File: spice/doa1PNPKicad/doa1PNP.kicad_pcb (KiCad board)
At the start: 2 copper layers, 27 parts, among them Q1 BC547, Q2 BC557, Q3 BC557, Q4 BC557, Q5 BC547, Q6 BC557, Q7 BC547

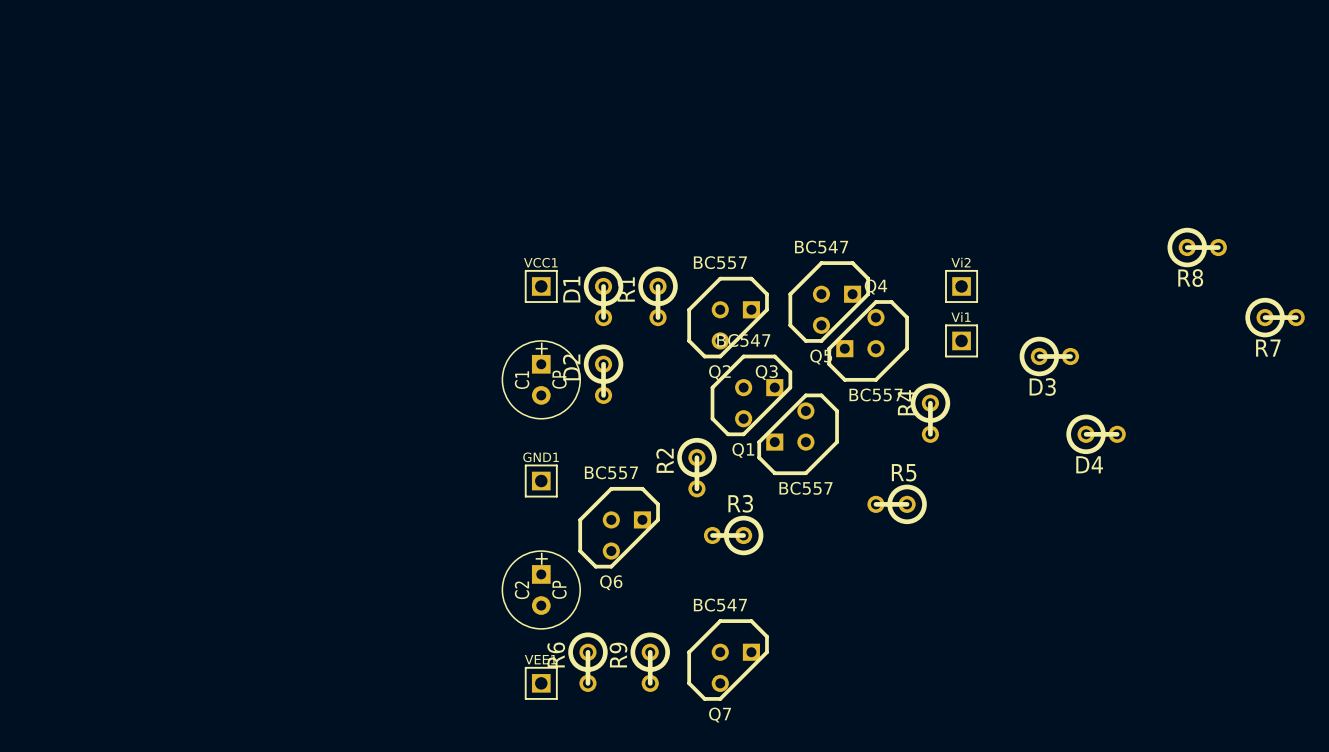
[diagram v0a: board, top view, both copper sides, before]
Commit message: multiple current source doa1PNP
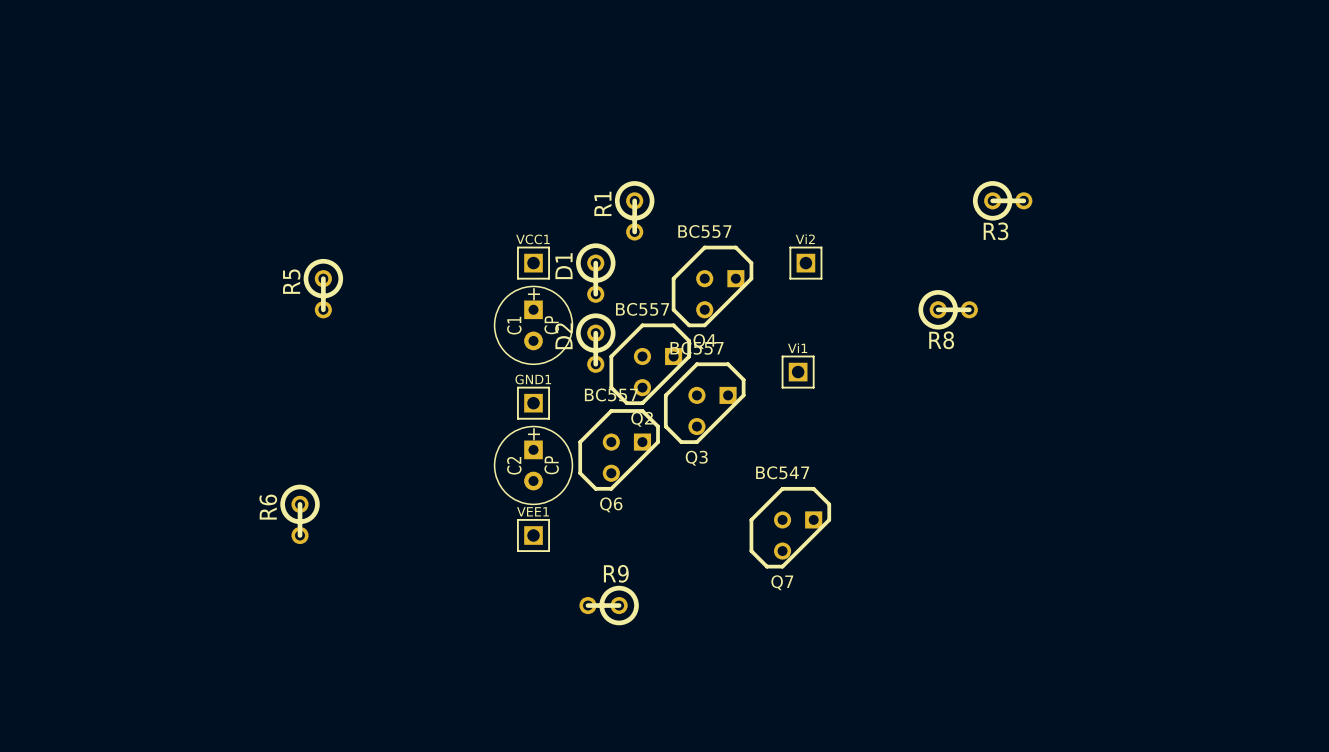
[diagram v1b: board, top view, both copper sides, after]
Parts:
- removed D3, D4: DIODE, R1
- removed Q1, Q5: BC547, TO92-123
- removed R2, R4, R7: R, R1
- moved R5 49.4 mm to (154.9, 108.6), turned to 270 degrees
- moved R3 35.6 mm to (210.8, 101.0), turned to 0 degrees
- moved R6 26.4 mm to (153.0, 127.0)
- moved R8 20.9 mm to (206.4, 109.9)
- moved Vi1 13.6 mm to (193.7, 114.9)
- moved Vi2 12.8 mm to (194.3, 106.0)
- moved VEE1 12.1 mm to (172.1, 128.3)
- moved Q7 11.9 mm to (193.7, 128.3)
- moved Q4 11.9 mm to (187.3, 108.6), turned to 0 degrees
- moved C2 10.2 mm to (172.1, 122.6)
- moved Q2 7.41 mm to (182.2, 114.9)
- moved R1 7.24 mm to (180.3, 102.2)
- moved Q3 6.48 mm to (186.7, 118.1), turned to 0 degrees
- moved GND1 6.38 mm to (172.1, 117.5)
- moved Q6 6.35 mm to (179.7, 121.9)
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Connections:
- D2 pad 2: N-000006 (its old number) -> N-000009
- Q2 pad 2: N-000006 (its old number) -> N-000009
- Q3 pad 1: N-0000013 (its old number) -> N-0000014
- Q4 pad 1: N-000008 (its old number) -> N-0000012
- Q6 pad 2: N-000001 (its old number) -> N-000009
- Q7 pad 2: N-0000017 -> N-0000012
- R3 pad 1: N-000009 -> N-0000014
- R5 pad 1: N-0000017 -> N-0000012
- R6 pad 1: N-000006 (its old number) -> N-000009
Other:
- board text removed: "Col"

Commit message: kicad out stage
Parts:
- added Q1: BC557, TO92-123, F.Cu at (137.2, 113.0)
- added Q5: BC557, TO92-123, F.Cu at (166.4, 92.7)
- added R2: R, R1, F.Cu at (149.9, 97.8)

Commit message: kicad out stage
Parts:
- moved Q5 37.0 mm to (134.6, 111.8)
- moved Q1 6.02 mm to (139.1, 107.3)
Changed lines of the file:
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@@
     (links 32)
     (no_connects 32)
-    (area 129.537178 81.6864 213.0425 135.849404)
+    (area 130.172178 95.925596 213.0425 135.849404)
     (thickness 1.6)
     (drawings 11)
@@
   )
   (module TO92-123 (layer F.Cu)
-    (at 166.37 92.71)
+    (at 134.62 111.76)
     (descr "Transistor TO92 brochage type BC237")
     (tags "TR TO92")
@@
   )
   (module TO92-123 (layer F.Cu)
-    (at 137.16 113.03)
+    (at 139.065 107.315)
     (descr "Transistor TO92 brochage type BC237")
     (tags "TR TO92")

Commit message: layout
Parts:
- removed Q1, Q2, Q6: BC557, TO92-123
- added Out1: CONN_1, PIN_ARRAY_1, F.Cu at (216.5, 119.4)
- added Q1CS3: BC557, TO92, F.Cu at (211.5, 120.7)
- added Q2CS1: BC557, TO92, F.Cu at (188.0, 118.7)
- added Q6CS2: BC557, TO92, F.Cu at (206.4, 116.2)
- C1, C2: footprint C1V7 -> C1
- moved Q5 78.1 mm to (210.8, 128.9)
- moved R2 63.6 mm to (212.7, 107.3), turned to 270 degrees
- moved R5 48.9 mm to (203.8, 109.2)
- moved C2 44.5 mm to (216.5, 123.8)
- moved GND1 44.5 mm to (216.5, 116.2)
- moved VCC1 44.5 mm to (216.5, 107.3)
- moved C1 44.5 mm to (216.5, 111.8)
- moved VEE1 44.4 mm to (216.5, 128.3)
- moved R3 42.9 mm to (172.1, 119.4), turned to 270 degrees
- moved R6 38.7 mm to (191.8, 127.0)
- moved R9 29.0 mm to (200.7, 116.2), turned to 90 degrees
- moved Vi2 27.3 mm to (180.3, 129.5)
- moved Vi1 22.0 mm to (177.2, 129.5)
- moved Q4 19.7 mm to (186.7, 128.3)
- moved Q7 11.4 mm to (203.8, 123.2), turned to 90 degrees
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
